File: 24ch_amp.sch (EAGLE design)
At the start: 151 parts, among them J1 TFM-125-02-XXX-D-WT, U1 TLE2426CD

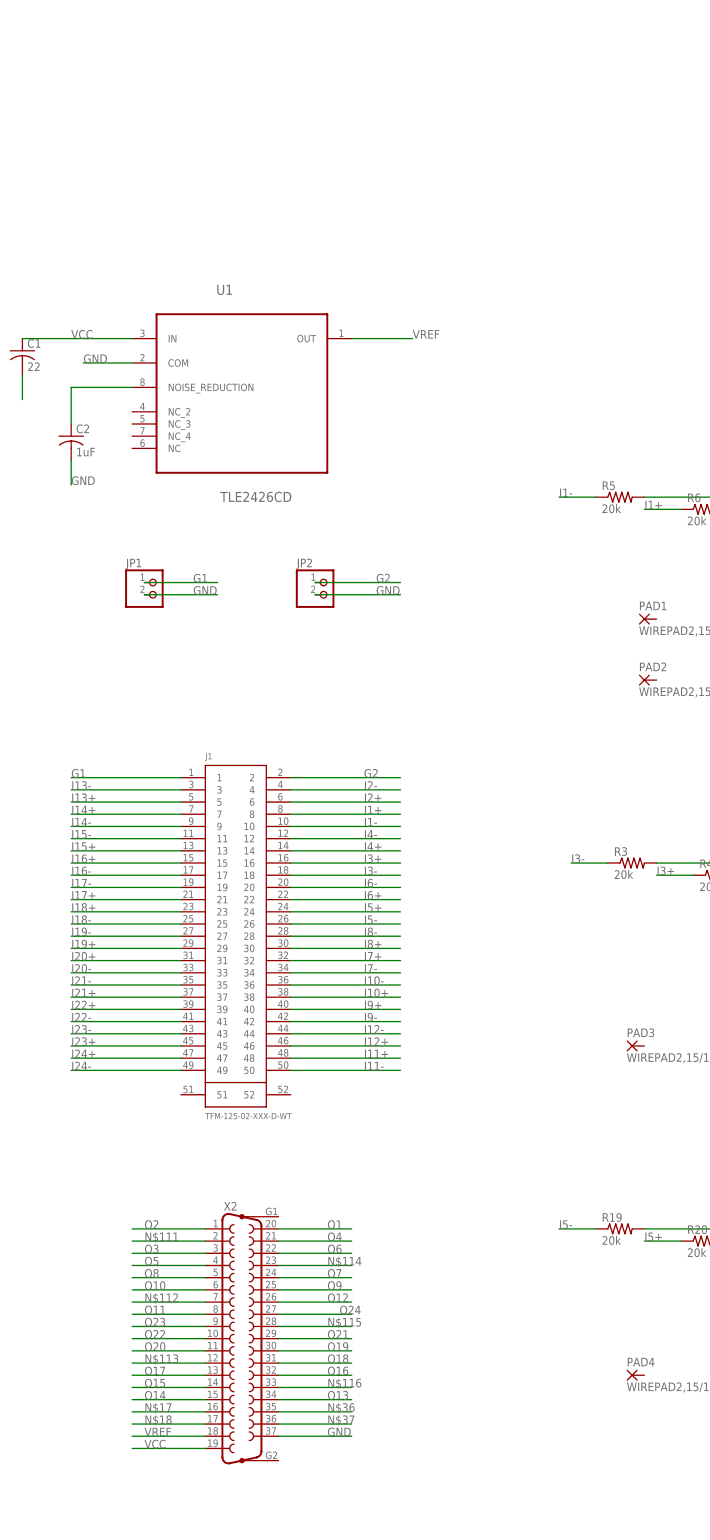
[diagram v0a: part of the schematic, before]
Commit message: minor updates to routing. Added DC-DC voltage converter/isolator to backplaneV2 & 24ch brd
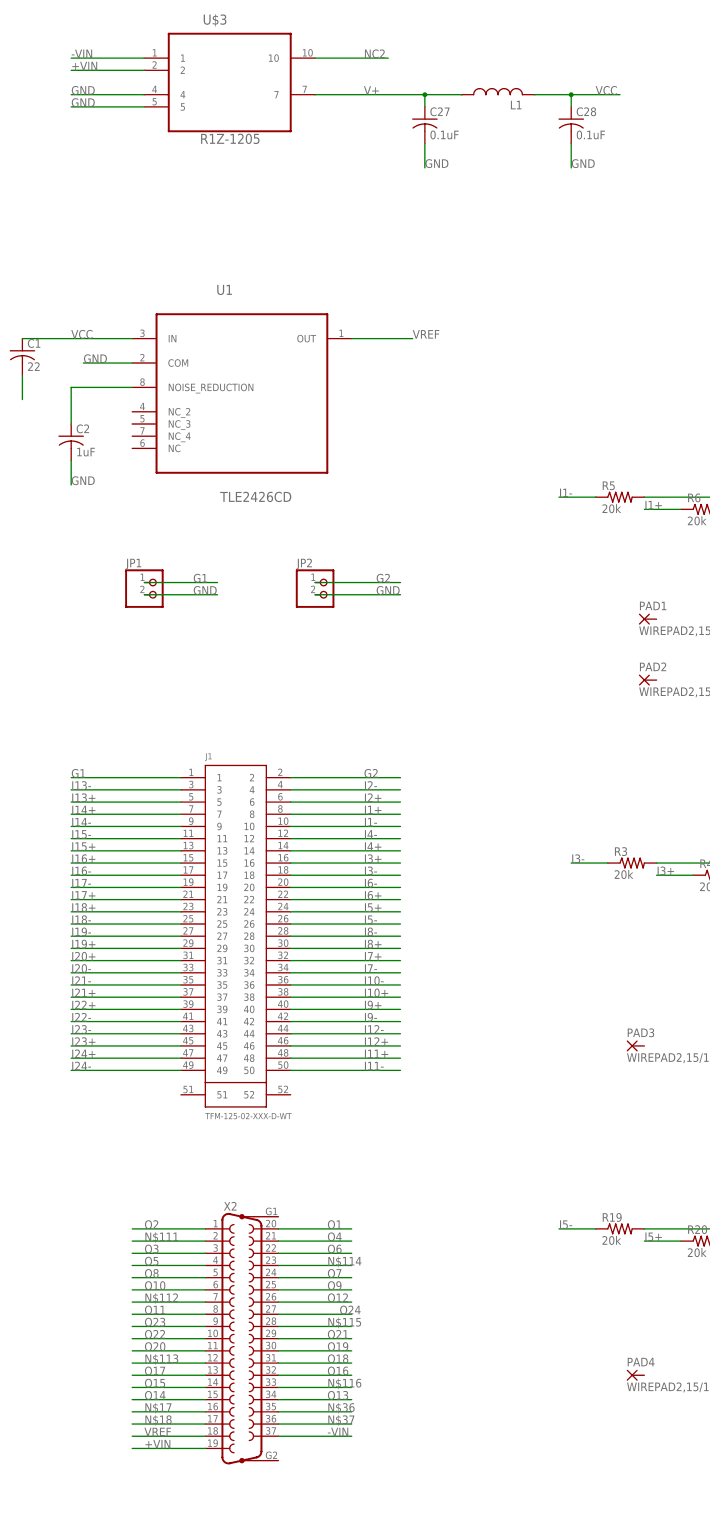
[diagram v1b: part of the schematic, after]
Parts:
- added C27, C28: 0.1uF, rcl:C-USC0805
- added L1: (no value), resistor:L-USL3225M
- added U$3: R1Z-1205, tuckerLib:R1Z-1205
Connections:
- new net +VIN: U$3.2, X2.19
- new net -VIN: U$3.1, X2.37
- new net NC2: U$3.10
- new net V+: C27.1, L1.1, U$3.7
- net GND: now also C27.2, C28.2, U$3.4, U$3.5; no longer X2.37
- net VCC: now also C28.1, L1.2; no longer X2.19
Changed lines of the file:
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@@
 <part name="R96" library="rcl" deviceset="R-US_" device="R0805" value="49.9"/>
 <part name="PAD12" library="wirepad" deviceset="WIREPAD" device="2,15/1,0" value="WIREPAD2,15/1,0"/>
+<part name="U$3" library="tuckerLib" deviceset="R1Z-1205" device=""/>
+<part name="L1" library="resistor" deviceset="L-US" device="L3225M"/>
+<part name="C27" library="rcl" deviceset="C-US" device="C0805" value="0.1uF"/>
+<part name="C28" library="rcl" deviceset="C-US" device="C0805" value="0.1uF"/>
 </parts>
 <sheets>
@@
 <instance part="R96" gate="G$1" x="363.22" y="109.22"/>
 <instance part="PAD12" gate="G$1" x="236.22" y="127"/>
+<instance part="U$3" gate="G$1" x="-20.32" y="208.28"/>
+<instance part="L1" gate="G$1" x="35.56" y="205.74" rot="R90"/>
+<instance part="C27" gate="G$1" x="20.32" y="200.66"/>
+<instance part="C28" gate="G$1" x="50.8" y="200.66"/>
 </instances>
 <busses>
@@
 <nets>
 <net name="GND" class="0">
-<segment>
-<pinref part="X2" gate="G$1" pin="37"/>
-<wire x1="-10.16" y1="-73.66" x2="5.08" y2="-73.66" width="0.1524" layer="91"/>
-<label x="0" y="-73.66" size="1.778" layer="95"/>
-</segment>
 <segment>
 <wire x1="-38.1" y1="101.6" x2="-22.86" y2="101.6" width="0.1524" layer="91"/>
@@
 <label x="287.02" y="114.3" size="1.778" layer="95"/>
 </segment>
+<segment>
+<pinref part="U$3" gate="G$1" pin="4"/>
+<wire x1="-38.1" y1="205.74" x2="-53.34" y2="205.74" width="0.1524" layer="91"/>
+<label x="-53.34" y="205.74" size="1.778" layer="95"/>
+</segment>
+<segment>
+<pinref part="U$3" gate="G$1" pin="5"/>
+<wire x1="-38.1" y1="203.2" x2="-53.34" y2="203.2" width="0.1524" layer="91"/>
+<label x="-53.34" y="203.2" size="1.778" layer="95"/>
+</segment>
+<segment>
+<pinref part="C27" gate="G$1" pin="2"/>
+<wire x1="20.32" y1="195.58" x2="20.32" y2="190.5" width="0.1524" layer="91"/>
+<label x="20.32" y="190.5" size="1.778" layer="95"/>
+</segment>
+<segment>
+<pinref part="C28" gate="G$1" pin="2"/>
+<wire x1="50.8" y1="195.58" x2="50.8" y2="190.5" width="0.1524" layer="91"/>
+<label x="50.8" y="190.5" size="1.778" layer="95"/>
+</segment>
 </net>
 <net name="I21+" class="0">
@@
 </net>
 <net name="VCC" class="0">
-<segment>
-<pinref part="X2" gate="G$1" pin="19"/>
-<wire x1="-25.4" y1="-76.2" x2="-40.64" y2="-76.2" width="0.1524" layer="91"/>
-<label x="-38.1" y="-76.2" size="1.778" layer="95"/>
-</segment>
 <segment>
 <pinref part="C6" gate="G$1" pin="1"/>
@@
 <wire x1="299.72" y1="111.76" x2="314.96" y2="111.76" width="0.1524" layer="91"/>
 <label x="302.26" y="111.76" size="1.778" layer="95"/>
+</segment>
+<segment>
+<pinref part="C28" gate="G$1" pin="1"/>
+<wire x1="50.8" y1="203.2" x2="50.8" y2="205.74" width="0.1524" layer="91"/>
+<pinref part="L1" gate="G$1" pin="2"/>
+<wire x1="50.8" y1="205.74" x2="43.18" y2="205.74" width="0.1524" layer="91"/>
+<wire x1="50.8" y1="205.74" x2="60.96" y2="205.74" width="0.1524" layer="91"/>
+<junction x="50.8" y="205.74"/>
+<label x="55.88" y="205.74" size="1.778" layer="95"/>
 </segment>
 </net>
@@
 </segment>
 </net>
+<net name="NC2" class="0">
+<segment>
+<pinref part="U$3" gate="G$1" pin="10"/>
+<wire x1="-2.54" y1="213.36" x2="12.7" y2="213.36" width="0.1524" layer="91"/>
+<label x="7.62" y="213.36" size="1.778" layer="95"/>
+</segment>
+</net>
+<net name="-VIN" class="0">
+<segment>
+<pinref part="U$3" gate="G$1" pin="1"/>
+<wire x1="-38.1" y1="213.36" x2="-53.34" y2="213.36" width="0.1524" layer="91"/>
+<label x="-53.34" y="213.36" size="1.778" layer="95"/>
+</segment>
+<segment>
+<pinref part="X2" gate="G$1" pin="37"/>
+<wire x1="-10.16" y1="-73.66" x2="5.08" y2="-73.66" width="0.1524" layer="91"/>
+<label x="0" y="-73.66" size="1.778" layer="95"/>
+</segment>
+</net>
+<net name="+VIN" class="0">
+<segment>
+<pinref part="U$3" gate="G$1" pin="2"/>
+<wire x1="-38.1" y1="210.82" x2="-53.34" y2="210.82" width="0.1524" layer="91"/>
+<label x="-53.34" y="210.82" size="1.778" layer="95"/>
+</segment>
+<segment>
+<pinref part="X2" gate="G$1" pin="19"/>
+<wire x1="-25.4" y1="-76.2" x2="-40.64" y2="-76.2" width="0.1524" layer="91"/>
+<label x="-38.1" y="-76.2" size="1.778" layer="95"/>
+</segment>
+</net>
+<net name="V+" class="0">
+<segment>
+<pinref part="U$3" gate="G$1" pin="7"/>
+<label x="7.62" y="205.74" size="1.778" layer="95"/>
+<pinref part="L1" gate="G$1" pin="1"/>
+<wire x1="-2.54" y1="205.74" x2="20.32" y2="205.74" width="0.1524" layer="91"/>
+<pinref part="C27" gate="G$1" pin="1"/>
+<wire x1="20.32" y1="205.74" x2="27.94" y2="205.74" width="0.1524" layer="91"/>
+<wire x1="20.32" y1="203.2" x2="20.32" y2="205.74" width="0.1524" layer="91"/>
+<junction x="20.32" y="205.74"/>
+</segment>
+</net>
